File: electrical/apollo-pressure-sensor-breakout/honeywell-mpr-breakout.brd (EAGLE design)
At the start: 25 x 36 mm, 12 parts, among them U1 HONEYWELL-MPR-SMD-GAUGE, X1 RJ45-8-2-CONEC-1, X2 M04X2

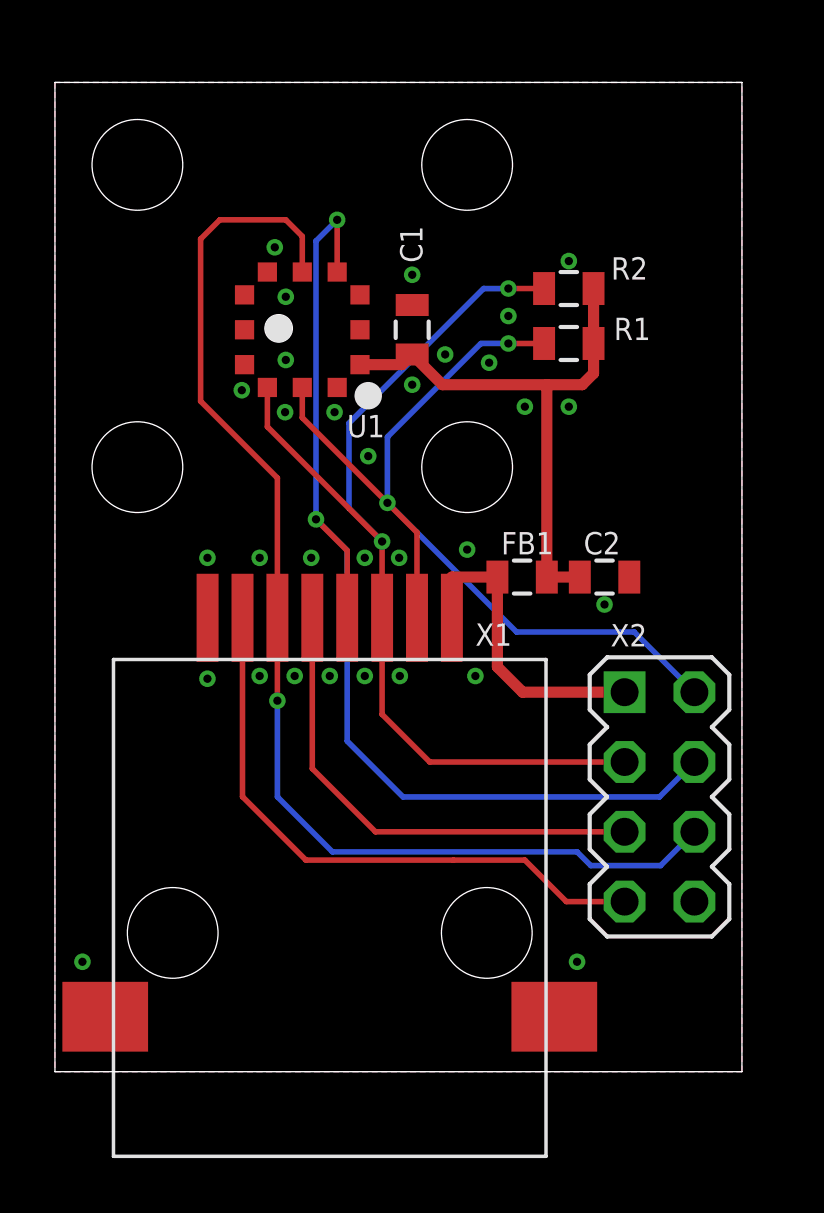
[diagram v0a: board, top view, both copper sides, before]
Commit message: added SPI signals to MPR breakout
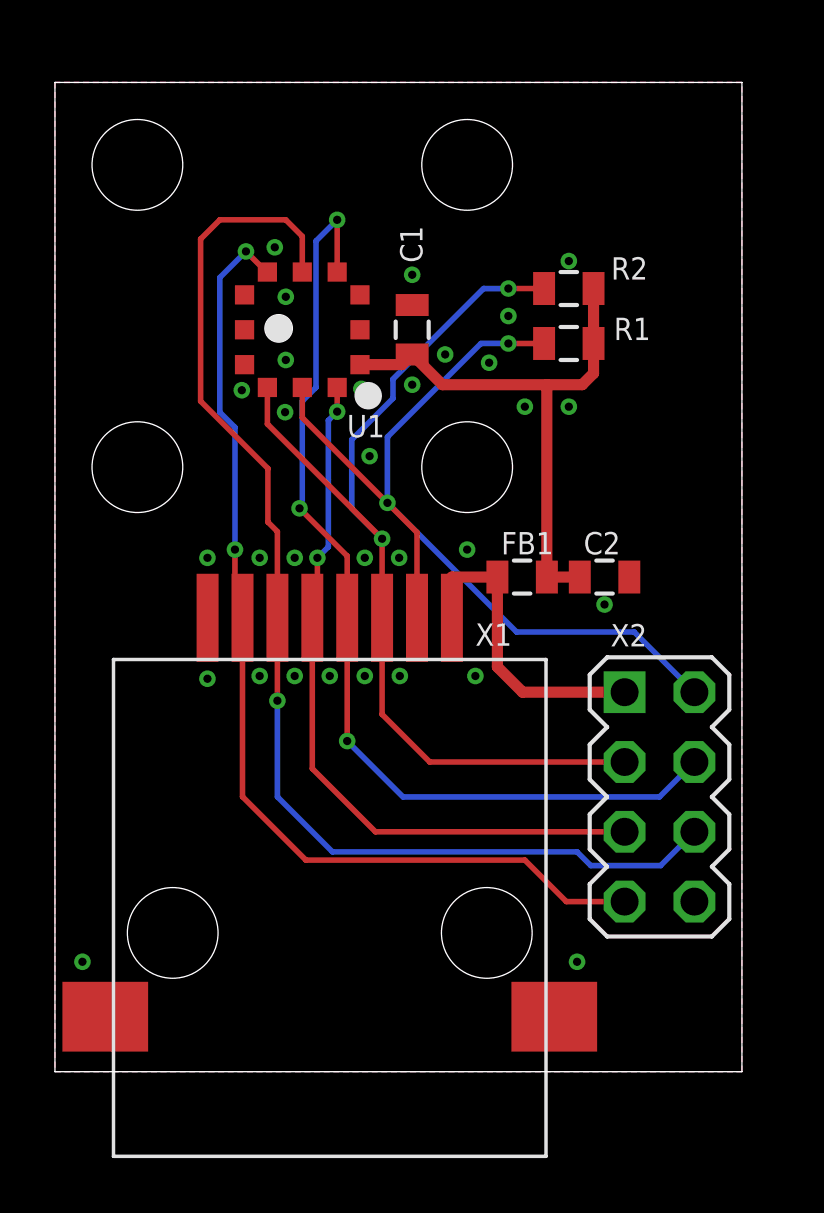
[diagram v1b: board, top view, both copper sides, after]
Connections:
- removed net AUX2: X1.7, X2.7
- new net MISO: U1.7, X1.7, X2.7
- net CS: now also U1.1
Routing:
- net MISO: track 0.00 -> 37.3 mm, vias 0 -> 2
- net AUX2: track 22.0 -> 0.00 mm
- net CS: track 17.8 -> 26.7 mm, vias 0 -> 2
- net RES: track 39.7 -> 36.2 mm, vias 2 -> 3

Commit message: resize MPR board, add mounting holes
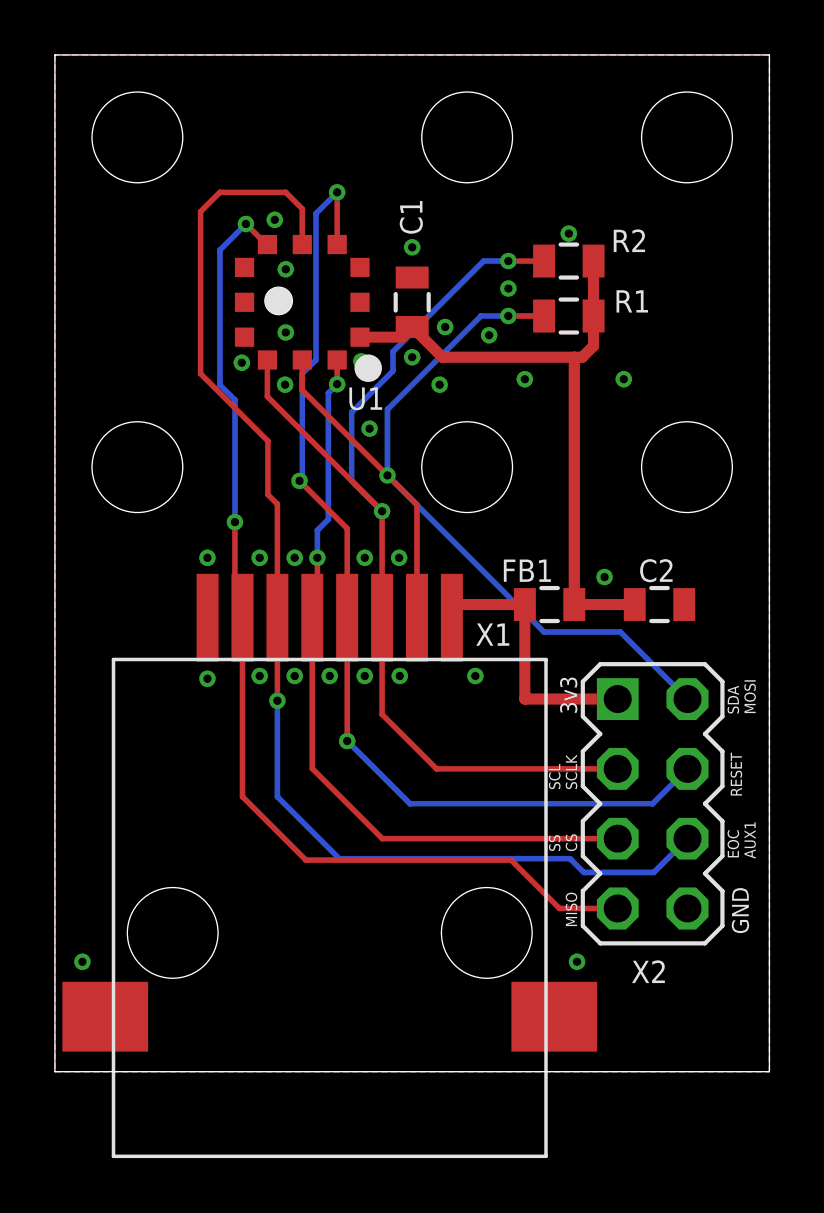
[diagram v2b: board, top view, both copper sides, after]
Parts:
- added JP5, JP6: STAND-OFF, apollo-ctrl:STAND-OFF
- moved C2 2.24 mm to (22.0, 17.0)
- moved FB1 1.41 mm to (18.0, 17.0)
- moved C1 1.00 mm to (13.0, 28.0)
- moved JP1 1.00 mm to (3.00, 34.0)
- moved JP2 1.00 mm to (15.0, 34.0)
- moved R1 1.00 mm to (18.7, 27.5)
- moved R2 1.00 mm to (18.7, 29.5)
- moved U1 1.00 mm to (9.00, 28.0)
- moved X2 0.35 mm to (21.8, 9.75)
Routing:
- net 3.3V: track 20.6 -> 23.6 mm
- net PWR: track 11.4 -> 9.96 mm
- net SDA: track 33.6 -> 34.9 mm
- net SCL: track 36.9 -> 37.8 mm
- net RES: track 36.2 -> 37.0 mm
- net MISO: track 37.3 -> 38.2 mm
- net AUX1: track 43.7 -> 44.6 mm
- net CS: track 26.7 -> 27.5 mm
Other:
- board size 25 x 36 mm -> 26 x 37 mm
- board text added: "3v3"
- board text added: "EOC AUX1"
- board text added: "GND"
- board text added: "MISO"
- board text added: "MPR sensor board Rev. C"
- board text added: "RESET"
- board text added: "SCL SCLK"
- board text added: "SDA MOSI"
- board text added: "SS CS"
